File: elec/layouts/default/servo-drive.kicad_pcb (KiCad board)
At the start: 4 copper layers, 42.3 x 42.3 mm, 109 parts

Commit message: layout complete
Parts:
- moved R41 61.3 mm to (162.2, 95.8)
- moved R35 60.6 mm to (146.5, 96.5), turned to 180 degrees
- moved R43 59.1 mm to (163.6, 95.8)
- moved R37 59.0 mm to (155.1, 95.9), turned to 90 degrees
- moved R33 58.6 mm to (148.3, 95.8), turned to 90 degrees
- moved R45 58.5 mm to (158.2, 100.9)
- moved R46 58.5 mm to (156.7, 100.9)
- moved R44 58.4 mm to (157.5, 98.1)
- moved C16 58.1 mm to (148.4, 84.8)
- moved C18 58.1 mm to (155.7, 85.0)
- moved C28 58.1 mm to (137.4, 97.3)
- moved C29 58.1 mm to (135.4, 97.3)
- moved C36 58.1 mm to (149.6, 107.1)
- moved C42 58.1 mm to (164.7, 88.2)
- moved C43 58.1 mm to (148.6, 99.1)
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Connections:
- J1 pad B5: servo_drive.ato/ServoDrive.gnd -> servo_drive.ato/ServoDrive.usb/cc2
- R20 pad 1: servo_drive.ato/ServoDrive/r_cc2/p1.ea763f -> servo_drive.ato/ServoDrive.usb/cc2
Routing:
- net servo_drive.ato/ServoDrive/power_stage/half_bridge_c.gate_driver/lvg: track 0.00 -> 3.00 mm
- net servo_drive.ato/ServoDrive/power_stage/half_bridge_b.gate_driver/lvg: track 0.00 -> 2.87 mm
- net servo_drive.ato/ServoDrive/position_sensor.sensor/PGO: track 0.00 -> 2.36 mm
- net servo_drive.ato/ServoDrive/power_stage/half_bridge_a.gate_driver/lvg: track 11.0 -> 13.2 mm, vias 2 -> 1
- net servo_drive.ato/ServoDrive/power_stage/half_bridge_c.ls_fet/gate: track 0.00 -> 1.38 mm
- net servo_drive.ato/ServoDrive/power_stage/half_bridge_b.ls_fet/gate: track 0.00 -> 1.34 mm
- net (no net): vias 17 -> 23
- added copper zone on F.Cu, net servo_drive.ato/ServoDrive.power_stage/out_b
- added copper zone on F.Cu, net servo_drive.ato/ServoDrive.power_stage/out_c
- added copper zone on F.Cu, net servo_drive.ato/ServoDrive.vbatt

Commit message: added git hash
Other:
- board size 42.3 x 42.3 mm -> 44.5 x 42.3 mm
- board text added: "{{GITHASH}}"
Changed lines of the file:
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@@
   (gr_arc (start 172.526046 81.083159) (mid 172.959569 81.73201) (end 173.111832 82.497372)
     (stroke (width 0.2) (type solid)) (layer "Edge.Cuts"))
+  (gr_line (start 128.644364 85.884116) (end 128.644364 100.510859)
+    (stroke (width 0.05) (type default)) (layer "Edge.Cuts"))
+  (gr_line (start 128.644364 85.884116) (end 130.814932 85.88399)
+    (stroke (width 0.05) (type default)) (layer "Edge.Cuts"))
   (gr_arc (start 130.811832 82.497372) (mid 130.964061 81.731998) (end 131.397619 81.083159)
     (stroke (width 0.2) (type solid)) (layer "Edge.Cuts"))
@@
   (gr_line (start 168.483405 77.868945) (end 135.44026 77.868945)
     (stroke (width 0.2) (type solid)) (layer "Edge.Cuts"))
+  (gr_line (start 130.811832 101.6) (end 130.811832 115.540518)
+    (stroke (width 0.05) (type default)) (layer "Edge.Cuts"))
   (gr_circle (center 136.461832 83.518945) (end 138.036832 83.518945)
     (stroke (width 0.2) (type solid)) (fill none) (layer "Edge.Cuts"))
-  (gr_line (start 130.811832 82.497372) (end 130.811832 115.540518)
+  (gr_line (start 130.811832 82.497372) (end 130.805433 85.67328)
     (stroke (width 0.2) (type solid)) (layer "Edge.Cuts"))
   (gr_line (start 172.526046 81.083159) (end 169.897619 78.454731)
@@
   (gr_arc (start 169.908069 119.617057) (mid 169.259219 120.050598) (end 168.493855 120.202843)
     (stroke (width 0.2) (type solid)) (layer "User.4"))
+  (gr_text "{{GITHASH}} " (at 172.390366 90.297516 90) (layer "F.SilkS")
+    (effects (font (size 1 1) (thickness 0.1)) (justify left bottom))
+  )
   (segment (start 144.481142 112.314225) (end 145.109339 112.314225) (width 0.09) (layer "F.Cu") (net 0))
   (segment (start 145.22138 112.48267) (end 145.371384 112.632674) (width 0.09) (layer "F.Cu") (net 0))
@@
       1bdba999-4030-44fa-9ed0-d660783914fa
       2b56ad7b-f105-4b26-a0a6-020b4eaadda2
+      2df787bb-b885-4557-b580-f7e08166d94a
       631cfb14-c48a-4a4d-b448-f55d9fd3540f
       686f4894-f635-4c7b-aa08-4d1bb6a9d7ab
@@
       86edfde9-809b-4ba1-9107-123cd53a899a
       8cba0fb0-03eb-4b1a-961f-170308723b54
+      93af2c3f-66ba-4ee8-b201-b478248fff0b
       afc4b192-368d-4522-b3ea-7e03c7956cbd
       c08dd099-f7d5-4be9-9f88-f2b7dc67a241

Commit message: more routing progress
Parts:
- C1: moved to F.Cu
- C34, C42: moved to B.Cu
- moved C34 27.8 mm to (134.6, 90.1), turned to 0 degrees
- moved C42 6.51 mm to (167.4, 94.1), turned to -90 degrees
- moved R35 3.37 mm to (143.4, 98.0)
- moved C3 3.21 mm to (167.8, 110.5), turned to 180 degrees
- moved R43 2.80 mm to (163.5, 98.6), turned to -90 degrees
- moved C43 2.37 mm to (148.2, 101.5), turned to -90 degrees
- moved C45 2.04 mm to (155.2, 101.3)
- moved C44 1.98 mm to (138.3, 93.0), turned to 90 degrees
- moved C1 1.75 mm to (154.9, 108.7), turned to -90 degrees
- moved R39 0.62 mm to (157.7, 97.1)
- moved R44 0.48 mm to (157.6, 98.6)
- moved R37 0.39 mm to (154.9, 96.2)
- moved R36 0.17 mm to (155.6, 90.7)
- moved U1 0.16 mm to (144.8, 83.8), turned to 180 degrees
- moved R3 0.16 mm to (171.0, 99.9)
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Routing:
- net servo_drive.ato/ServoDrive.v_3: track 0.00 -> 46.1 mm, vias 0 -> 2
- net servo_drive.ato/ServoDrive/power_stage.half_v_ref: track 0.00 -> 42.6 mm, vias 0 -> 3
- net servo_drive.ato/ServoDrive.v_10: track 0.00 -> 25.5 mm
- net servo_drive.ato/ServoDrive.gnd: track 0.00 -> 19.0 mm, vias 0 -> 46
- net servo_drive.ato/ServoDrive/micro_kit.boot_vdiv/output-flash/ncs-micro/qspi_ss_n: track 15.9 -> 32.2 mm, vias 0 -> 1
- net servo_drive.ato/ServoDrive.vbatt: track 0.00 -> 11.3 mm, vias 0 -> 10
- net servo_drive.ato/ServoDrive/power_stage/half_bridge_b.gate_driver/hvg: track 0.00 -> 10.1 mm, vias 0 -> 2
- net servo_drive.ato/ServoDrive/power_stage/half_bridge_a.gate_driver/lvg: track 13.2 -> 3.10 mm, vias 1 -> 0
- net servo_drive.ato/ServoDrive/power_stage/half_bridge_a.ls_fet/gate: track 1.62 -> 9.85 mm, vias 0 -> 1
- net servo_drive.ato/ServoDrive/power_stage/half_bridge_c.ls_fet/gate: track 1.38 -> 8.59 mm, vias 0 -> 1
- net (no net): track 6.22 -> 0.00 mm, vias 23 -> 11
- net servo_drive.ato/ServoDrive/micro_kit.micro/xin-osc/in: track 0.00 -> 5.80 mm
- net servo_drive.ato/ServoDrive.power_stage/out_a: track 0.00 -> 5.41 mm
- net servo_drive.ato/ServoDrive.power_stage/out_b: track 0.00 -> 4.87 mm
- net servo_drive.ato/ServoDrive.voltage_input_vdiv/out: track 0.00 -> 4.71 mm
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- added copper zone on B.Cu, net servo_drive.ato/ServoDrive.gnd
- added copper zone on F.Cu, net servo_drive.ato/ServoDrive.gnd
- added copper zone on In2.Cu, net servo_drive.ato/ServoDrive.gnd
- added copper zone on F.Cu, net servo_drive.ato/ServoDrive.v_10
- added copper zone on F.Cu, net servo_drive.ato/ServoDrive/buck.buck_converter/LX

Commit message: Routing almost complete
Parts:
- moved R40 14.2 mm to (163.9, 88.0), turned to -90 degrees
- moved C38 5.82 mm to (152.2, 111.0)
- moved R31 1.53 mm to (133.8, 110.0), turned to 180 degrees
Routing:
- net servo_drive.ato/ServoDrive.power_stage/i_fb_a: track 0.00 -> 37.6 mm, vias 0 -> 3
- net servo_drive.ato/ServoDrive.power_stage/i_fb_c: track 0.00 -> 33.3 mm, vias 0 -> 3
- net servo_drive.ato/ServoDrive.power_stage/i_fb_b: track 0.00 -> 32.2 mm, vias 0 -> 3
- net servo_drive.ato/ServoDrive.voltage_input_vdiv/out: track 4.71 -> 33.6 mm, vias 0 -> 2
- net servo_drive.ato/ServoDrive.gnd: track 19.0 -> 44.1 mm, vias 46 -> 106
- net servo_drive.ato/ServoDrive.v_10: track 25.5 -> 46.2 mm, vias 0 -> 1
- net servo_drive.ato/ServoDrive.v_3: track 46.1 -> 65.3 mm, vias 2 -> 7
- net servo_drive.ato/ServoDrive/power_stage/half_bridge_c.gate_driver/hvg: track 0.00 -> 17.0 mm, vias 0 -> 2
- net servo_drive.ato/ServoDrive/micro_kit.micro/usb_dm: track 0.00 -> 15.5 mm
- net servo_drive.ato/ServoDrive/micro_kit/micro.iovdd: track 0.00 -> 14.4 mm
- net servo_drive.ato/ServoDrive/micro_kit.micro/usb_dp: track 0.00 -> 14.2 mm
- net servo_drive.ato/ServoDrive/power_stage.current_sense_b/i_in-half_bridge_b/out: track 0.00 -> 13.9 mm, vias 0 -> 9
- net servo_drive.ato/ServoDrive/power_stage.current_sense_c/i_in-half_bridge_c/out: track 0.00 -> 13.7 mm, vias 0 -> 9
- net servo_drive.ato/ServoDrive/buck.SGND: track 3.86 -> 14.9 mm, vias 0 -> 2
- net servo_drive.ato/ServoDrive/power_stage.current_sense_a/i_in-half_bridge_a/out: track 19.3 -> 27.9 mm, vias 1 -> 10
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- added copper zone on In1.Cu, net servo_drive.ato/ServoDrive.gnd
- added copper zone on In1.Cu, net servo_drive.ato/ServoDrive.v_3
- added copper zone on B.Cu, net servo_drive.ato/ServoDrive/power_stage.current_sense_a/i_in-half_bridge_a/out
- added copper zone on F.Cu, net servo_drive.ato/ServoDrive/power_stage.current_sense_a/i_in-half_bridge_a/out
- added copper zone on B.Cu, net servo_drive.ato/ServoDrive/power_stage.current_sense_b/i_in-half_bridge_b/out
- added copper zone on F.Cu, net servo_drive.ato/ServoDrive/power_stage.current_sense_b/i_in-half_bridge_b/out
- added copper zone on B.Cu, net servo_drive.ato/ServoDrive/power_stage.current_sense_c/i_in-half_bridge_c/out
- added copper zone on F.Cu, net servo_drive.ato/ServoDrive/power_stage.current_sense_c/i_in-half_bridge_c/out
- removed copper zone on B.Cu, net servo_drive.ato/ServoDrive.power_stage/out_a
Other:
- outline, holes or cut-outs redrawn

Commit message: Routing complete
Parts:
- removed R3: 10kOhm, Resistor_SMD:R_0402_1005Metric
- moved R29 0.18 mm to (133.7, 103.7)
- moved C17 0.14 mm to (162.1, 81.4)
- moved R5 0.14 mm to (148.2, 86.6)
- moved C30 0.12 mm to (133.7, 101.5)
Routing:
- net servo_drive.ato/ServoDrive.v_3: track 65.3 -> 157.0 mm
- net servo_drive.ato/ServoDrive/power_stage.current_sense_b/i_in-half_bridge_b/out: track 13.9 -> 32.1 mm, vias 9 -> 10
- net servo_drive.ato/ServoDrive.gnd: track 44.1 -> 61.9 mm, vias 106 -> 114
- net servo_drive.ato/ServoDrive/micro_kit.micro/dvdd-micro/vreg_vout: track 7.17 -> 24.2 mm, vias 2 -> 3
- net servo_drive.ato/ServoDrive/power_stage.current_sense_c/i_in-half_bridge_c/out: track 13.7 -> 30.0 mm, vias 9 -> 10
- net servo_drive.ato/ServoDrive/micro_kit/micro.iovdd: track 14.4 -> 25.0 mm
- net servo_drive.ato/ServoDrive/usb.sbu: track 0.00 -> 8.71 mm
- net servo_drive.ato/ServoDrive/power_stage/half_bridge_c.hs_fet/gate: track 0.00 -> 7.26 mm, vias 0 -> 1
- net servo_drive.ato/ServoDrive.position_sensor/scl: track 23.5 -> 18.2 mm
- net servo_drive.ato/ServoDrive.position_sensor/sda: track 25.6 -> 20.8 mm
- net servo_drive.ato/ServoDrive/micro_kit.flash/do-micro/qspi_sd1: track 14.8 -> 10.1 mm
- net servo_drive.ato/ServoDrive.power_stage/low_in_b: track 15.1 -> 18.4 mm
- net servo_drive.ato/ServoDrive/power_stage.current_sense_a/i_in-half_bridge_a/out: track 27.9 -> 30.9 mm
- net servo_drive.ato/ServoDrive/micro_kit.flash/io2-micro/qspi_sd2: track 13.4 -> 16.1 mm
- net servo_drive.ato/ServoDrive/power_stage/current_sense_b.amp/in_n: track 5.85 -> 7.32 mm
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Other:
- board size 44.5 x 42.3 mm -> 46 x 42.3 mm
- board text added: "BOOT"
- board text added: "RUN"
- board text added: "https://gitlab.atopile.io/atopile/servo-drive"

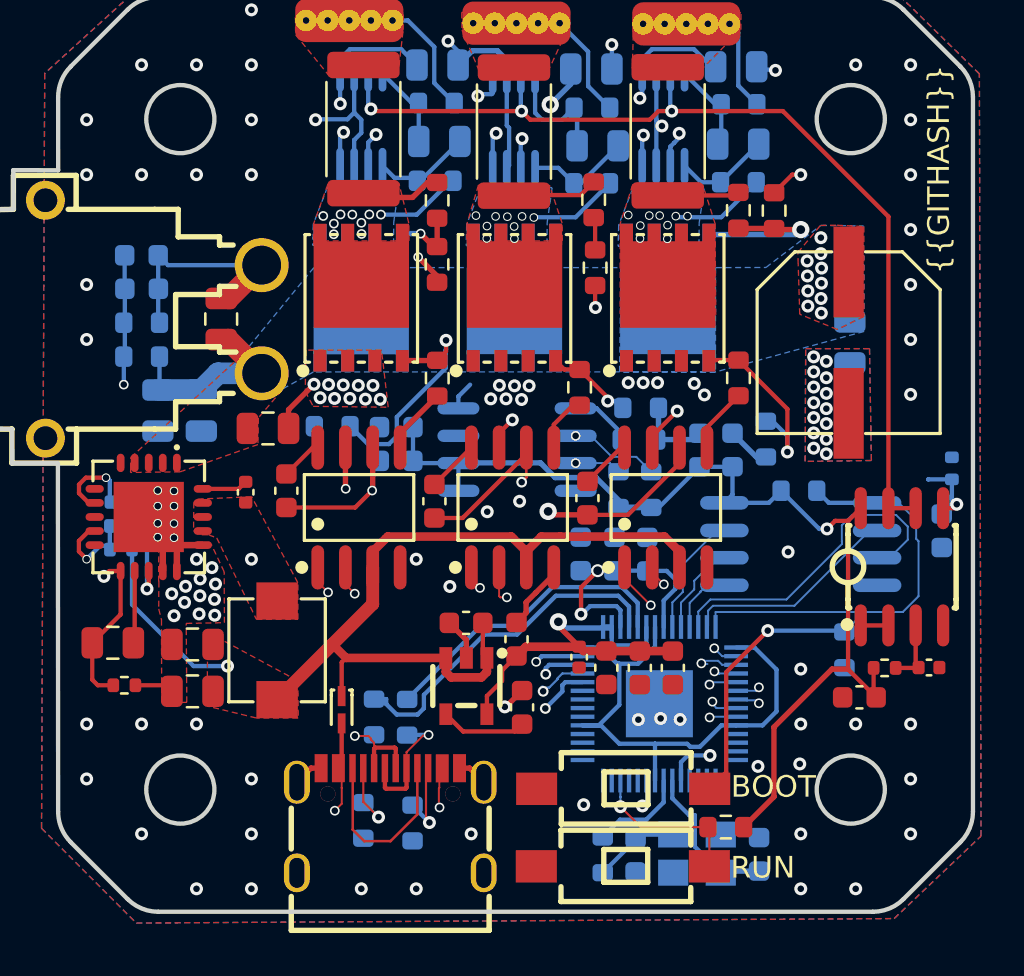
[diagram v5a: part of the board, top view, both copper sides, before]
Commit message: Most DRC errors fixed
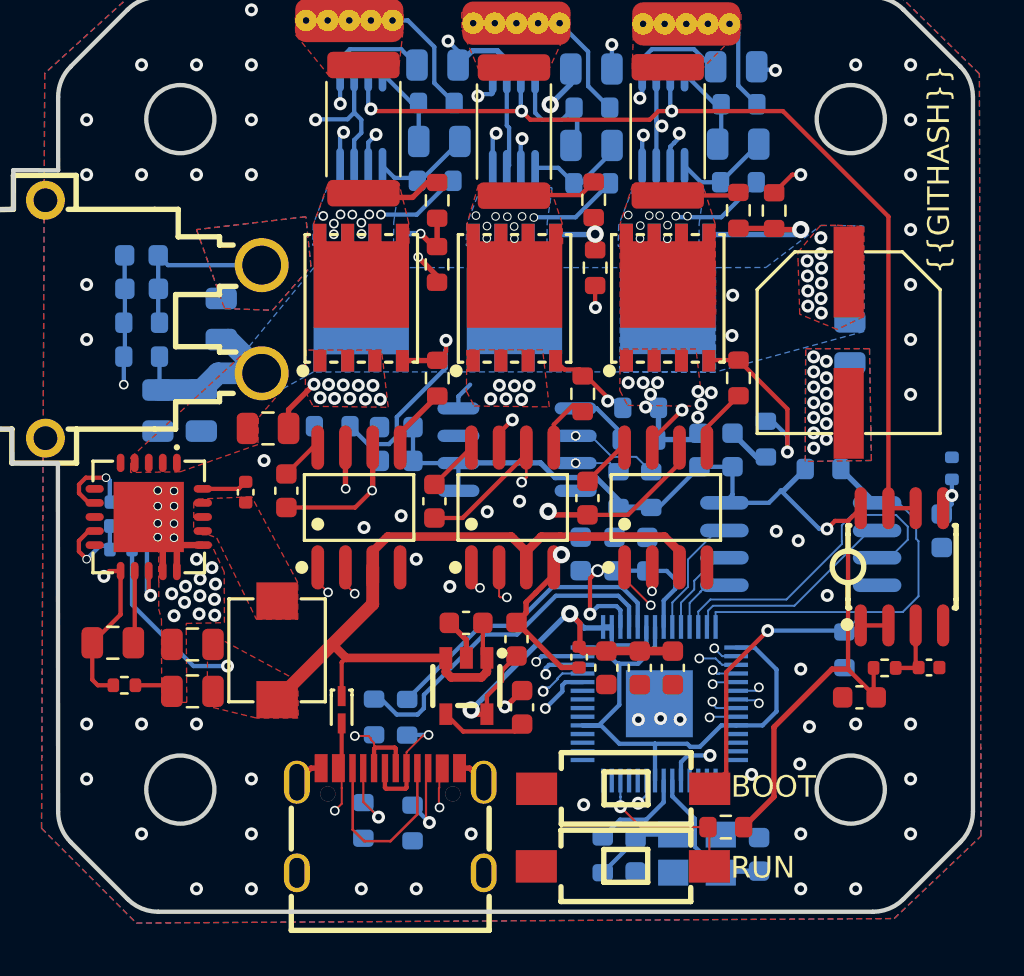
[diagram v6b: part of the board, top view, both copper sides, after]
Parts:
- C44: moved to B.Cu
- moved R14 1.50 mm to (166.1, 100.0)
- moved R37 0.33 mm to (155.0, 96.5)
- moved C18 0.28 mm to (155.4, 85.0)
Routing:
- net servo_drive.ato/ServoDrive.v_3: track 157.0 -> 161.9 mm, vias 7 -> 8
- net servo_drive.ato/ServoDrive/power_stage/ref.buffer/in_p_b-half_ref/output: track 4.50 -> 2.55 mm
- net servo_drive.ato/ServoDrive/power_stage/half_bridge_b.hs_fet/gate: track 1.52 -> 3.36 mm, vias 0 -> 1
- net servo_drive.ato/ServoDrive.gnd: track 61.9 -> 63.2 mm, vias 114 -> 124
- net servo_drive.ato/ServoDrive/buck.SGND: track 14.9 -> 15.8 mm
- net servo_drive.ato/ServoDrive/micro_kit.micro/dvdd-micro/vreg_vout: track 24.2 -> 23.5 mm
- net servo_drive.ato/ServoDrive/micro_kit.boot_vdiv/output-flash/ncs-micro/qspi_ss_n: track 32.2 -> 31.5 mm
